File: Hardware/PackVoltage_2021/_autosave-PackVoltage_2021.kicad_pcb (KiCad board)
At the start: 2 copper layers, 152.4 x 177.8 mm, 139 parts, among them J3V1 Test_Point, J5V1 Test_Point, Q1 BUK7M8R5-40HX, Q10 BUK7M8R5-40HX, Q2 BUK7M8R5-40HX, Q3 BUK7M8R5-40HX, Q4 BUK7M8R5-40HX, Q5 BUK7M8R5-40HX, Q6 BUK7M8R5-40HX, Q7 BUK7M8R5-40HX, Q8 BUK7M8R5-40HX, Q9 BUK7M8R5-40HX, U1 LT1910, U10 INA281, U12 OKI-78SR-3.3_1.5-W36-C, U13 OKI-78SR-5_1.5-W36-C, U14 LT1910, U15 LT1910, U16 LT1910, U17 INA281, U18 INA281, U19 INA281, U2 LT1910, U20 LT1910, U21 LT1910, U22 INA281, U23 INA281, U24 TM4C129E_Launchpad, U3 LT1910, U4 INA281, U5 INA281, U6 INA281, U7 LT1910, U8 LT1910, U9 INA281

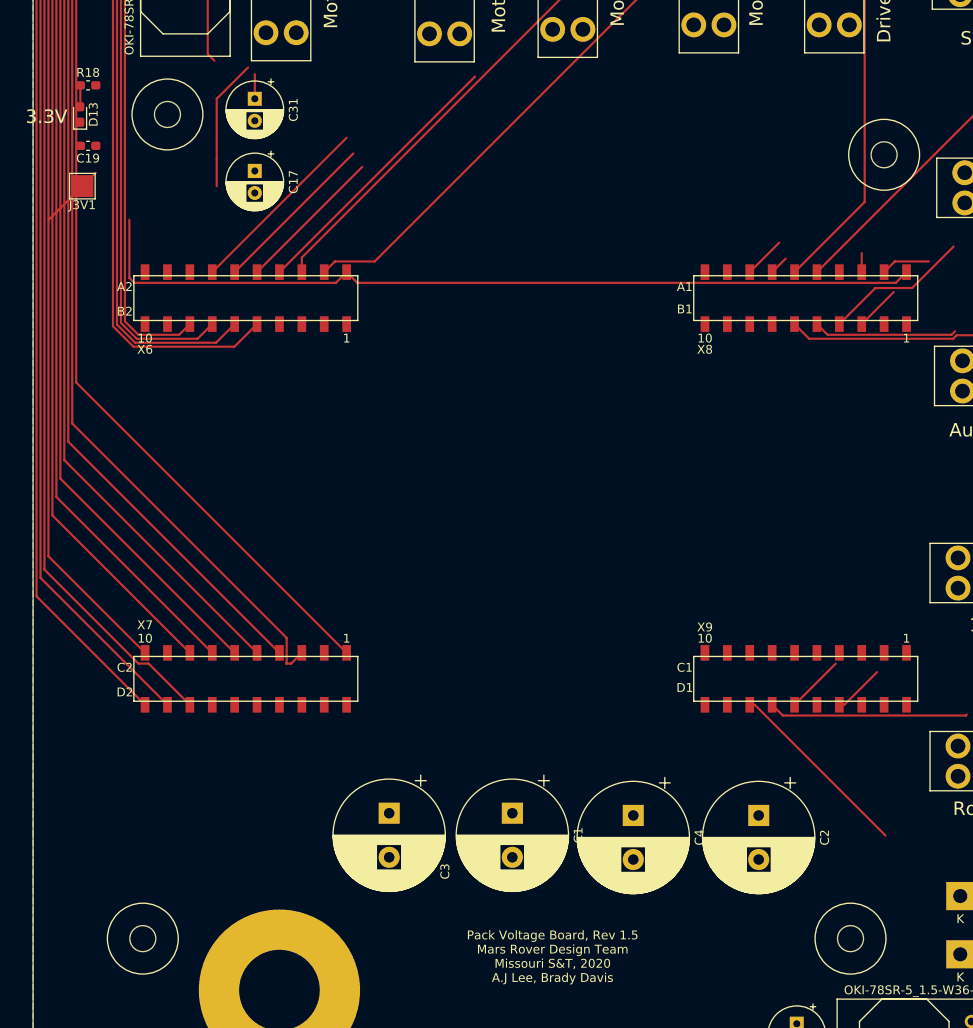
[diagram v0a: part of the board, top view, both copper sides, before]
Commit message: updated mosfet footprints
but for real this time
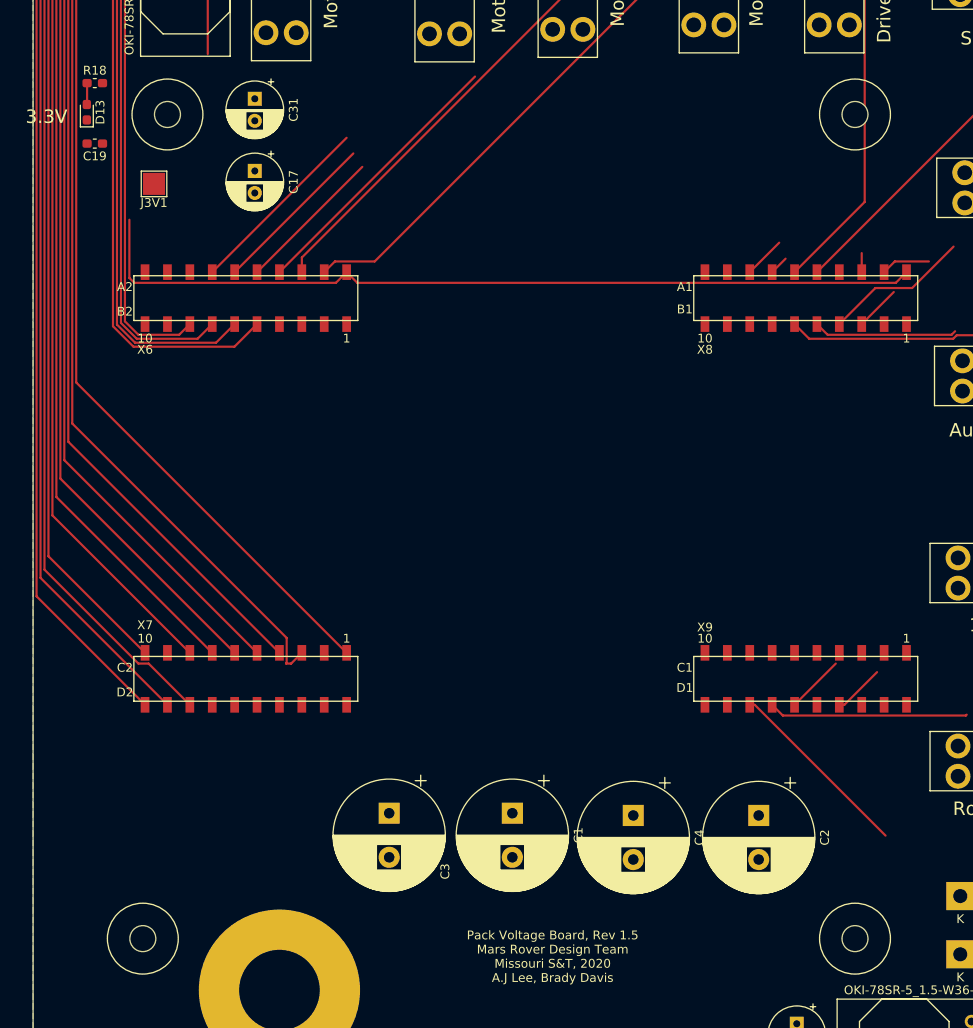
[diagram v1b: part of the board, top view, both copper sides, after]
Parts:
- removed the REF** at (172.7, 67.8)
- removed the REF** at (168.9, 156.7)
- added REF**: 4_40_Hole, MRDT_Drill_Holes:4_40_Hole, F.Cu at (169.4, 63.2)
- added REF**: 4_40_Hole, MRDT_Drill_Holes:4_40_Hole, F.Cu at (169.4, 156.7)
- moved J3V1 8.13 mm to (89.9, 71.1)
- moved C19 0.80 mm to (83.2, 66.5)
- moved D13 0.80 mm to (82.3, 63.0)
- moved R18 0.80 mm to (83.2, 59.7)
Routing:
- net +3V3: track 137.8 -> 111.5 mm
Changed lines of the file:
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@@
     (thickness 1.6)
     (drawings 21)
-    (tracks 117)
+    (tracks 110)
     (zones 0)
     (modules 139)
@@
   )
   (module MRDT_Drill_Holes:4_40_Hole (layer F.Cu)
-    (at 172.72 67.818)
+    (at 169.418 63.246)
     (clearance 2.54)
-    (fp_text reference REF** (at -0.00508 0.50508) (layer F.SilkS) hide
+    (fp_text reference REF** (at 0 0.50508) (layer F.SilkS) hide
       (effects (font (size 1 1) (thickness 0.15)))
     )
@@
   )
   (module MRDT_Drill_Holes:4_40_Hole (layer F.Cu)
-    (at 168.91 156.718)
+    (at 169.418 156.718)
     (clearance 2.54)
     (fp_text reference REF** (at -0.00508 0.50508) (layer F.SilkS) hide
@@
   )
   (module Capacitor_SMD:C_0603_1608Metric_Pad1.05x0.95mm_HandSolder (layer F.Cu)
-    (at 82.437 66.802 180)
+    (at 83.199 66.548 180)
     (descr "Capacitor SMD 0603 (1608 Metric), square (rectangular) end terminal, IPC_7351 nominal with elongated pad for handsoldering. (Body size source: http://www.tortai-tech.com/upload/download/2011102023233369053.pdf), generated with kicad-footprint-generator")
     (tags "capacitor handsolder")
@@
   )
   (module LED_SMD:LED_0603_1608Metric_Pad1.05x0.95mm_HandSolder (layer F.Cu)
-    (at 81.534 63.246 90)
+    (at 82.296 62.992 90)
     (descr "LED SMD 0603 (1608 Metric), square (rectangular) end terminal, IPC_7351 nominal, (Body size source: http://www.tortai-tech.com/upload/download/2011102023233369053.pdf), generated with kicad-footprint-generator")
     (tags "LED handsolder")
@@
   )
   (module TestPoint:TestPoint_Pad_2.5x2.5mm (layer F.Cu)
-    (at 81.788 71.374 180)
+    (at 89.916 71.12 180)
     (descr "SMD rectangular pad as test Point, square 2.5mm side length")
     (tags "test point SMD pad rectangle square")
@@
   )
   (module Resistor_SMD:R_0603_1608Metric_Pad1.05x0.95mm_HandSolder (layer F.Cu)
-    (at 82.437 59.944)
+    (at 83.199 59.69)
     (descr "Resistor SMD 0603 (1608 Metric), square (rectangular) end terminal, IPC_7351 nominal with elongated pad for handsoldering. (Body size source: http://www.tortai-tech.com/upload/download/2011102023233369053.pdf), generated with kicad-footprint-generator")
     (tags "resistor handsolder")
@@
   (segment (start 192.278 169.164) (end 190.246 171.196) (width 0.25) (layer F.Cu) (net 9) (status 20))
   (segment (start 134.733 9.539) (end 134.747 9.525) (width 0.25) (layer F.Cu) (net 9))
-  (segment (start 100.584 57.912) (end 97.028 61.468) (width 0.25) (layer F.Cu) (net 10))
   (segment (start 96.012 41.402) (end 96.012 56.388) (width 0.25) (layer F.Cu) (net 10))
-  (segment (start 96.774 57.15) (end 96.012 56.388) (width 0.25) (layer F.Cu) (net 10))
-  (segment (start 101.346 61.468) (end 101.346 58.674) (width 0.25) (layer F.Cu) (net 10))
-  (segment (start 97.028 61.468) (end 97.028 68.326) (width 0.25) (layer F.Cu) (net 10))
-  (segment (start 83.312 69.85) (end 81.788 71.374) (width 0.25) (layer F.Cu) (net 10))
-  (segment (start 97.028 68.326) (end 97.028 71.374) (width 0.25) (layer F.Cu) (net 10))
-  (segment (start 81.788 71.374) (end 77.978 75.184) (width 0.25) (layer F.Cu) (net 10))
   (segment (start 87.675601 82.341601) (end 110.545999 82.341601) (width 0.25) (layer F.Cu) (net 10))
   (segment (start 87.122 81.788) (end 87.675601 82.341601) (width 0.25) (layer F.Cu) (net 10))
@@
   (segment (start 76.592926 16.371074) (end 76.592926 117.893326) (width 0.25) (layer F.Cu) (net 92))
   (segment (start 81.28 11.684) (end 76.592926 16.371074) (width 0.25) (layer F.Cu) (net 92) (status 10))
-  (segment (start 81.562 62.343) (end 81.534 62.371) (width 0.25) (layer F.Cu) (net 94))
-  (segment (start 81.562 59.944) (end 81.562 62.343) (width 0.25) (layer F.Cu) (net 94))
+  (segment (start 82.324 62.089) (end 82.296 62.117) (width 0.25) (layer F.Cu) (net 94))
+  (segment (start 82.324 59.69) (end 82.324 62.089) (width 0.25) (layer F.Cu) (net 94))
   (segment (start 81.093019 93.640619) (end 111.76 124.3076) (width 0.25) (layer F.Cu) (net 109) (status 20))
   (segment (start 92.964 24.384) (end 92.964 24.468762) (width 0.25) (layer F.Cu) (net 109) (status 30))
